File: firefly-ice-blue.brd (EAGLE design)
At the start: 34 x 33.5 mm, 120 parts, among them J1 USB-5PINZX62WD1-B-5PC, J2 CON-6SOCKET, U1 EFM32LG330F256, U10 STM6519, U11 TPS782XX, U12 TPS6208X, U13 NX3L1T53, U14 FDFMA2P029Z, U16 MEMORY-SPIWLBGA-8, U17 ADP151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

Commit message: add test fixture board
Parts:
- added R12: 100k, firefly:R0201
- R14, R5: value 0 (DNS) -> 0 (OPT)
- R6: value 50 -> 25
- R8: value 20k -> 12.4k
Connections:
- net BAT_V: now also U14.3; no longer U14.4
- net GND: now also R12.2
- net USB_VBUS: now also R12.1
- net VUNREG: now also U14.4; no longer U14.3, U14.C, U14.D
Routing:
- net USB_VBUS: track 41.2 -> 43.2 mm
- net VUNREG: track 64.2 -> 65.7 mm, vias 8 -> 9
- net BAT_V: track 25.7 -> 25.0 mm, vias 2 -> 3
- net GND: track 90.2 -> 90.4 mm, vias 113 -> 114
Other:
- board text added: "Ice Blue 1.4"
- board text removed: "Ice Blue 1.3"

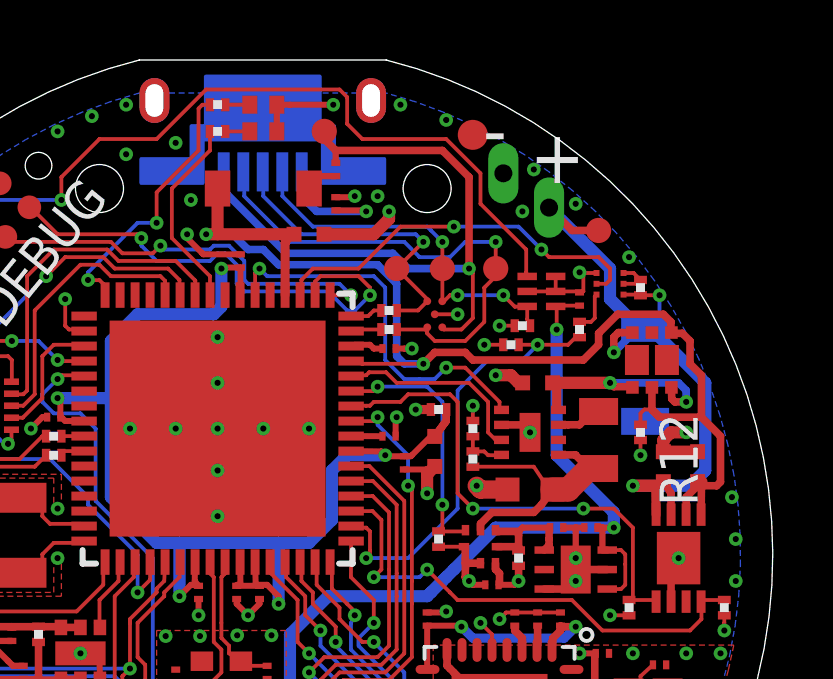
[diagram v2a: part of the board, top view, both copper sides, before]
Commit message: raise voltage to 2.5V; make external usb id reset optional
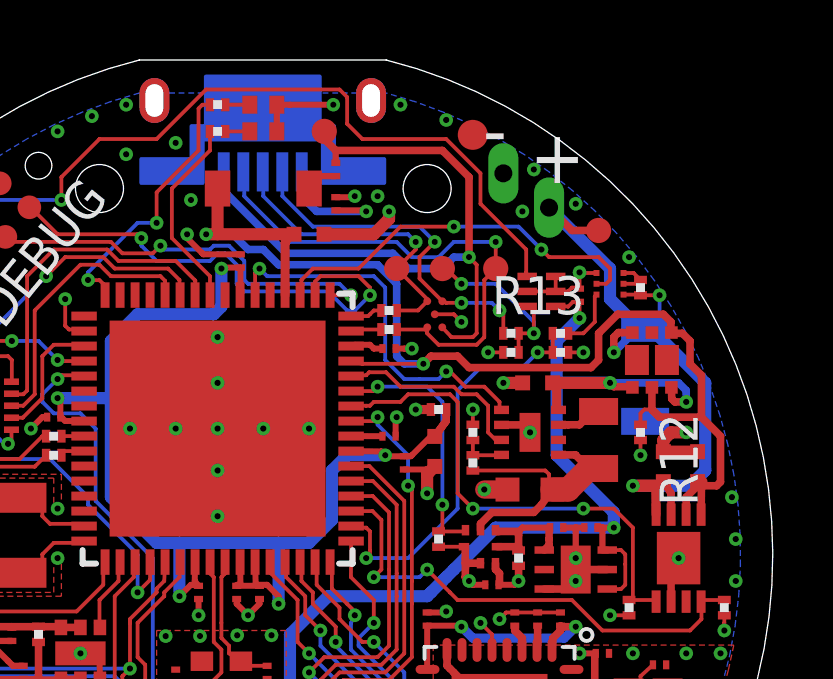
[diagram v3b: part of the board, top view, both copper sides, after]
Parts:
- added R13: 0 (OPT), firefly:R0201
- R3: value 152.4k -> 182k
- moved R32 1.67 mm to (26.9, 23.7), turned to 0 degrees
- moved R2 0.97 mm to (25.3, 23.7)
- moved R31 0.65 mm to (26.9, 24.4), turned to 180 degrees
- moved R3 0.13 mm to (24.0, 20.1)
- moved C9 0.13 mm to (27.6, 25.7)
- moved R10 0.13 mm to (24.0, 21.1)
- renumbered USBID to EXTRESET
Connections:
- new net N$14: EXTRESET.1, R13.2, R2.2, U10.3
- net N$8: now also R13.1; no longer EXTRESET.1, R2.2, U10.3
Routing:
- net N$14: track 0.00 -> 6.42 mm, vias 0 -> 2
- net BAT_V/2: track 14.7 -> 13.6 mm
- net GND: track 90.4 -> 89.5 mm
- net N$38: track 21.9 -> 22.7 mm
- net N$8: track 12.5 -> 11.9 mm
- net N$60: track 1.37 -> 1.98 mm
- net VUNREG: track 65.7 -> 66.2 mm

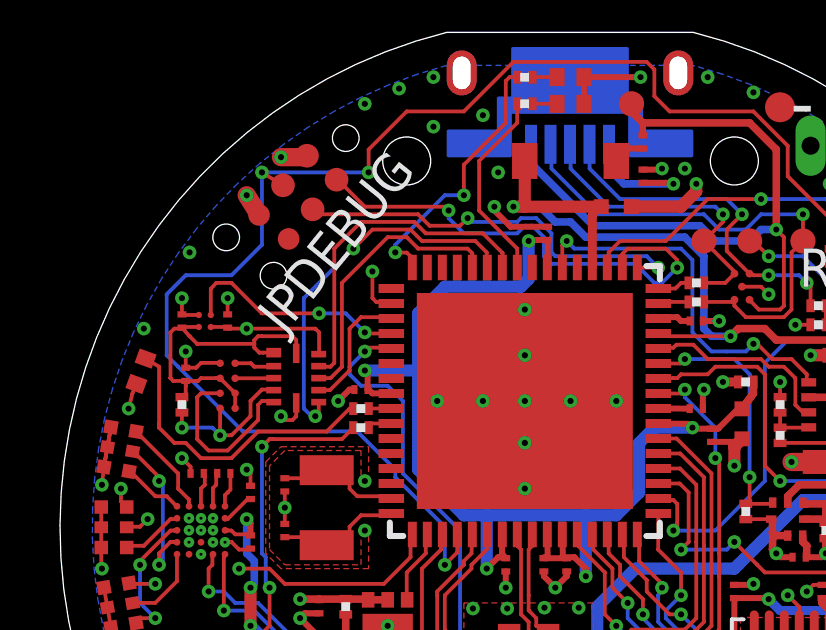
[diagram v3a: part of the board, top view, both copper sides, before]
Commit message: add accelerometer interrupt to pin 5 (since pin 4 can't be shared due to radio use)
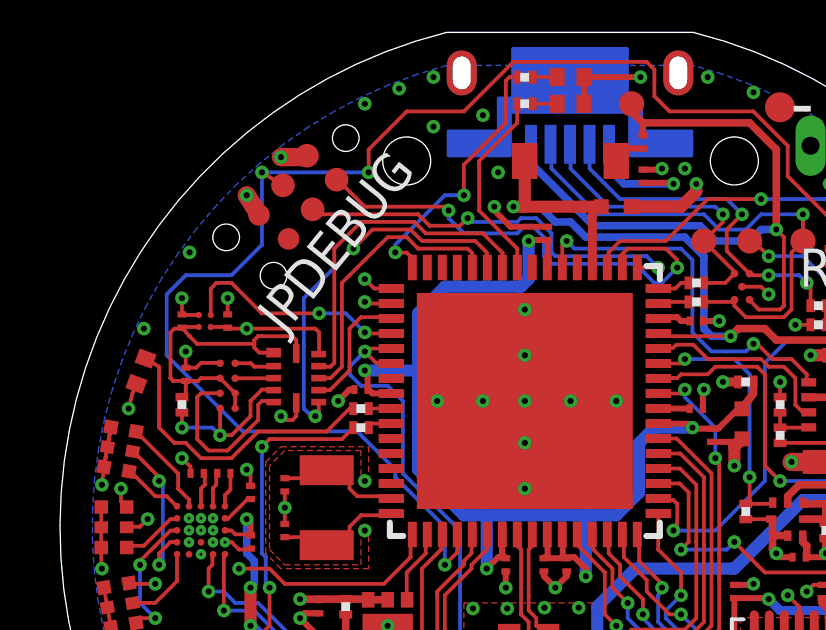
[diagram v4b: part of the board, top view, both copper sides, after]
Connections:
- net ACC_INT: now also U1.6
- net VCC: now also U1.1
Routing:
- net CLK32K: track 23.9 -> 22.5 mm
- net ACC_INT: track 21.4 -> 22.5 mm
- net VCC: track 40.0 -> 41.0 mm, vias 19 -> 20
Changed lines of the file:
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@@
 <layer number="13" name="Route13" color="4" fill="5" visible="no" active="no"/>
 <layer number="14" name="Route14" color="1" fill="6" visible="no" active="no"/>
-<layer number="15" name="Route15" color="13" fill="1" visible="no" active="yes"/>
+<layer number="15" name="Route15" color="13" fill="1" visible="yes" active="yes"/>
 <layer number="16" name="Bottom" color="3" fill="1" visible="yes" active="yes"/>
 <layer number="17" name="Pads" color="2" fill="1" visible="yes" active="yes"/>
@@
 <wire x1="8.636" y1="23.495" x2="8.636" y2="22.783" width="0.127" layer="1"/>
 <wire x1="8.636" y1="22.783" x2="8.624" y2="22.771" width="0.127" layer="1"/>
+<contactref element="U1" pad="1"/>
+<via x="10.16" y="25.273" extent="1-16" drill="0.2032"/>
+<wire x1="11.044" y1="24.959" x2="10.474" y2="24.959" width="0.127" layer="1"/>
+<wire x1="10.474" y1="24.959" x2="10.16" y2="25.273" width="0.127" layer="1"/>
 </signal>
 <signal name="N$25">
@@
 <signal name="ACC_INT">
 <contactref element="U3" pad="11"/>
-<contactref element="U1" pad="5"/>
-<wire x1="11.044" y1="22.959" x2="10.894" y2="22.959" width="0.127" layer="1"/>
-<wire x1="10.894" y1="22.959" x2="10.795" y2="22.987" width="0.127" layer="1"/>
-<wire x1="10.795" y1="22.987" x2="10.287" y2="22.987" width="0.127" layer="1"/>
-<wire x1="10.287" y1="22.987" x2="10.16" y2="22.86" width="0.127" layer="1"/>
+<wire x1="10.795" y1="22.479" x2="10.541" y2="22.479" width="0.127" layer="1"/>
+<wire x1="10.541" y1="22.479" x2="10.16" y2="22.86" width="0.127" layer="1"/>
 <via x="10.16" y="22.86" extent="1-16" drill="0.2032"/>
 <wire x1="10.16" y1="22.86" x2="9.652" y2="22.352" width="0.127" layer="16"/>
@@
 <via x="17.526" y="8.89" extent="1-16" drill="0.2032"/>
 <wire x1="17.526" y1="8.89" x2="17.526" y2="9.963" width="0.127" layer="1"/>
+<contactref element="U1" pad="6"/>
+<wire x1="10.795" y1="22.479" x2="11.044" y2="22.479" width="0.127" layer="1"/>
+<wire x1="11.044" y1="22.479" x2="11.044" y2="22.459" width="0.127" layer="1"/>
+<contactref element="U1" pad="5"/>
+<wire x1="11.044" y1="22.959" x2="10.287" y2="22.959" width="0.127" layer="1"/>
+<wire x1="10.287" y1="22.959" x2="10.16" y2="22.86" width="0.127" layer="1"/>
 </signal>
 <signal name="NRF_RDYN">
@@
 <wire x1="20.828" y1="17.399" x2="13.462" y2="17.399" width="0.127" layer="15"/>
 <wire x1="13.462" y1="17.399" x2="11.938" y2="18.923" width="0.127" layer="15"/>
-<wire x1="11.938" y1="18.923" x2="11.938" y2="24.003" width="0.127" layer="15"/>
-<wire x1="11.938" y1="24.003" x2="10.414" y2="25.527" width="0.127" layer="15"/>
-<via x="10.414" y="25.527" extent="1-16" drill="0.2032"/>
-<wire x1="10.414" y1="25.527" x2="10.414" y2="24.638" width="0.127" layer="1"/>
-<wire x1="10.414" y1="24.638" x2="10.541" y2="24.511" width="0.127" layer="1"/>
-<wire x1="10.541" y1="24.511" x2="10.992" y2="24.511" width="0.127" layer="1"/>
-<wire x1="10.992" y1="24.511" x2="11.044" y2="24.459" width="0.127" layer="1"/>
+<wire x1="11.938" y1="18.923" x2="11.938" y2="22.987" width="0.127" layer="15"/>
+<wire x1="11.938" y1="22.987" x2="10.414" y2="24.511" width="0.127" layer="15"/>
+<wire x1="10.414" y1="24.511" x2="10.16" y2="24.511" width="0.127" layer="15"/>
+<via x="10.16" y="24.511" extent="1-16" drill="0.2032"/>
+<wire x1="11.044" y1="24.459" x2="10.287" y2="24.459" width="0.127" layer="1"/>
+<wire x1="10.287" y1="24.459" x2="10.16" y2="24.511" width="0.127" layer="1"/>
 </signal>
 <signal name="N$3">
